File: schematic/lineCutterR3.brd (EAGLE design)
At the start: 55.9 x 30.5 mm, 53 parts, among them IC2 MC33269ST-3.3T3, J1 10118192-0001LF, Q1 AO4576, Q2 AO4576, Q3 DMG2305, Q4 AO4576, SW1 KMR2, U1 MS560702BA03-50, U2 MDBT50Q, U3 S25FL128SDPMFIG13S03016, U4 ESP32-S2-WROVER, U5 KXTJ3-1057, X1 2x5 0.05", X2 PIN-HEADER-MICRO-2-5-SMD

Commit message: Add Buck/Boost, RGB, Continuity, current sense
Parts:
- removed C20, C21, C5: .1u, rcl:C0805
- removed C3: 10u, rcl:C0805
- removed D1: MBR120, microbuilder:SOD-123
- removed IC2: MC33269ST-3.3T3, linear:SOT223
- removed JP1: JUMPER-SMT_2_NO_SILK, SparkFun-Jumpers:SMT-JUMPER_2_NO_SILK
- removed Q3: DMG2305, microbuilder:SOT23-R
- removed U5: KXTJ3-1057, Line Cutter COTS:KIONIX_KXTJ3-1057
- removed VCUT1, VCUT2: (no value), pinhead:1X02
- removed X2: PIN-HEADER-MICRO-2-5-SMD, freescale-uc:PIN-HEADER-NICRO-2-5-SMD
- added C10, C13, C14: 10u, rcl:C0805
- added C11, C15, C16: .1u, rcl:C0805
- added D2: XZM2CRKM2DGFBB45SCCB, SparkFun-LED:PLCC4SMDLED
- added D3: MBR120, microbuilder:SOD-123
- added H3, VCUT_1, VCUT_2: MOUNT-PAD-ROUND2.8, holes:2,8-PAD
- added L1: NR3015T1R5N, Line Cutter COTS:NR3015T1R5N
- added PS1: TPS63031DSKR, Line Cutter COTS:SON50P250X250X80-11N
- added Q5: DMG2305, microbuilder:SOT23-R
- added R18, R19, R20, R21: 10k, rcl:R0805
- added R22: 100k, rcl:R0805
- added R23, R24: 330, rcl:R0805
- added U6: ICM-20602, Line Cutter COTS:PQFN50P300X300X80-16N
- C9: value 4.7u -> .1u
- R17: value 100K -> 10k; device microbuilder:RESPACK_4X0603 -> rcl:R0805
- R7: value 10k -> 330
- U4: value ESP32-S2-WROVER -> ACS711KEXLT-31AB-T; device Line Cutter COTS:MODULE_ESP32-S2-WROVER -> Line Cutter COTS:SENSOR_ACS711KEXLT-31AB-T
- moved R7 204.8 mm to (-76.2, -177.2), flipped to the top
- moved C9 129.1 mm to (-52.7, -71.8), flipped to the top, turned to 0 degrees
- moved R16 107.3 mm to (78.7, -16.5), turned to 180 degrees
- moved R15 100.2 mm to (74.3, -16.5), turned to 180 degrees
- moved X1 87.6 mm to (7.62, 12.1), turned to 0 degrees
- moved SW1 84.6 mm to (14.0, 4.45), turned to 180 degrees
- moved R10 84.3 mm to (24.1, 22.2)
- moved R4 81.2 mm to (-32.4, 16.5), turned to 0 degrees
- moved CHG1 77.0 mm to (-32.4, 12.7), flipped to the bottom
- moved R9 76.9 mm to (19.1, 22.2)
- moved C12 74.9 mm to (-32.4, 8.89), turned to 180 degrees
- moved C1 74.7 mm to (74.3, 33.7), flipped to the top, turned to 180 degrees
- moved R3 73.4 mm to (-32.4, 3.81)
- moved CHG 69.9 mm to (-32.4, 6.35), turned to 90 degrees
- moved J1 67.6 mm to (22.4, 25.3), turned to 180 degrees
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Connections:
- removed net BL-RESET: R7.1, U4.41, X2.P$10
- removed net BOOT0: JP1.2, U4.3
- removed net IO38_DBLTAP: U4.32
- removed net TCK: U4.33, X2.P$4
- removed net TDI: U4.35, X2.P$8
- removed net TDO: U4.34, X2.P$6
- removed net TMS_D42: U4.36, X2.P$2
- removed net VHI: C20.2, C3.2, D1.C, IC2.3, Q3.2
- new net CUT_SENSE1: R18.1, R19.1, U2.9
- new net CUT_SENSE2: R20.1, R21.1, U2.20
- new net LED_B: R23.1, U2.44
- new net LED_G: R7.1, U2.42
- new net LED_R: R24.1, U2.41
- new net N$14: R17.1, U4.6
- new net N$15: D2.2, R7.2
- new net N$17: Q1.P$5, Q1.P$6, Q1.P$7, Q1.P$8, R18.2, VCUT_1.B2,8
- new net N$18: C11.2, PS1.6, PS1.7, PS1.8
- new net N$19: L1.2, PS1.4
- new net N$20: L1.1, PS1.2
- new net N$21: D2.1, R24.2
- new net N$22: C16.2, U6.14
- new net VBAT_IN_RAW: LIPO.1, Q4.P$4, U4.1
- new net VIN_REG1: C10.2, D3.C, PS1.5, Q5.2
- new net V_CURR_SENSE: U4.11
- net 3.3V: now also C13.2, C14.2, C15.2, PS1.1, PS1.10, R17.2, U4.12, U6.1, U6.16, U6.4, U6.5; no longer C21.2, C5.2, IC2.2, IC2.4, R7.2, U4.2, U5.10, U5.11, U5.3, U5.7, X2.P$1
- net CS0: no longer U4.20
- net CUT1: no longer U4.4
- net CUT2: no longer U4.5
- net GND: now also C10.1, C11.1, C13.1, C14.1, C15.1, C16.1, D2.4, PS1.11, PS1.3, PS1.9, R19.2, R21.2, R22.1, U4.10, U4.5, U4.7, U4.8, U4.9, U6.10, U6.11, U6.12, U6.13, U6.15, U6.8, U6.9; no longer C20.1, C21.1, C3.1, C5.1, IC2.1, JP1.1, R17.8, U4.1, U4.26, U4.42, U4.43_1, U4.43_10, U4.43_11, U4.43_12, U4.43_13, U4.43_14, U4.43_15, U4.43_16, U4.43_17, U4.43_18, U4.43_19, U4.43_2, U4.43_20, U4.43_21, U4.43_3, U4.43_4, U4.43_5, U4.43_6, U4.43_7, U4.43_8, U4.43_9, U5.1, U5.4, U5.6, U5.8, U5.9, X2.P$3, X2.P$5, X2.P$7, X2.P$9
- net MISO: no longer U4.31
- net MOSI: no longer U4.29
- net N$16: now also D2.3, R23.2; no longer Q1.P$5, Q1.P$6, Q1.P$7, Q1.P$8, VCUT1.1
- net N$6: now also R20.2, VCUT_2.B2,8; no longer VCUT2.1
- net SCK: no longer U4.30
- net SCL: now also U6.2; no longer U4.28, U5.12
- net SDA: now also U6.3; no longer U4.27, U5.2
- net USB_D+: no longer U4.23
- net USB_D-: no longer U4.22
- net VBAT: now also H3.B2,8, Q5.3, U4.3; no longer LIPO.1, Q3.3, Q4.P$4, VCUT1.2, VCUT2.2
- net VUSB: now also D3.A, Q5.1, R22.2; no longer D1.A, Q3.1, R17.1
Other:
- board size 55.9 x 30.5 mm -> 50.8 x 29.2 mm

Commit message: final code for cert rocket tests
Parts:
- moved C12 67.3 mm to (34.9, 8.89)
- moved CHG 67.3 mm to (34.9, 6.35)
- moved CHG1 67.3 mm to (34.9, 12.7)
- moved R3 67.3 mm to (34.9, 3.81)
- moved R4 67.3 mm to (34.9, 16.5)
- moved D3 45.3 mm to (43.2, 10.5)
- moved PS1 45.2 mm to (43.8, 13.3)
- moved Q5 44.5 mm to (43.8, 8.00)
- moved L1 44.3 mm to (39.4, 14.0)
- moved C1 43.2 mm to (39.4, 8.26)
- moved Q2 19.7 mm to (18.4, 3.81)
- moved D2 3.59 mm to (34.9, 20.3)
- moved U1 3.59 mm to (30.5, 14.6), turned to 180 degrees
- moved Q1 3.24 mm to (10.8, 3.81)
- moved SW1 3.24 mm to (10.8, 3.81)
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
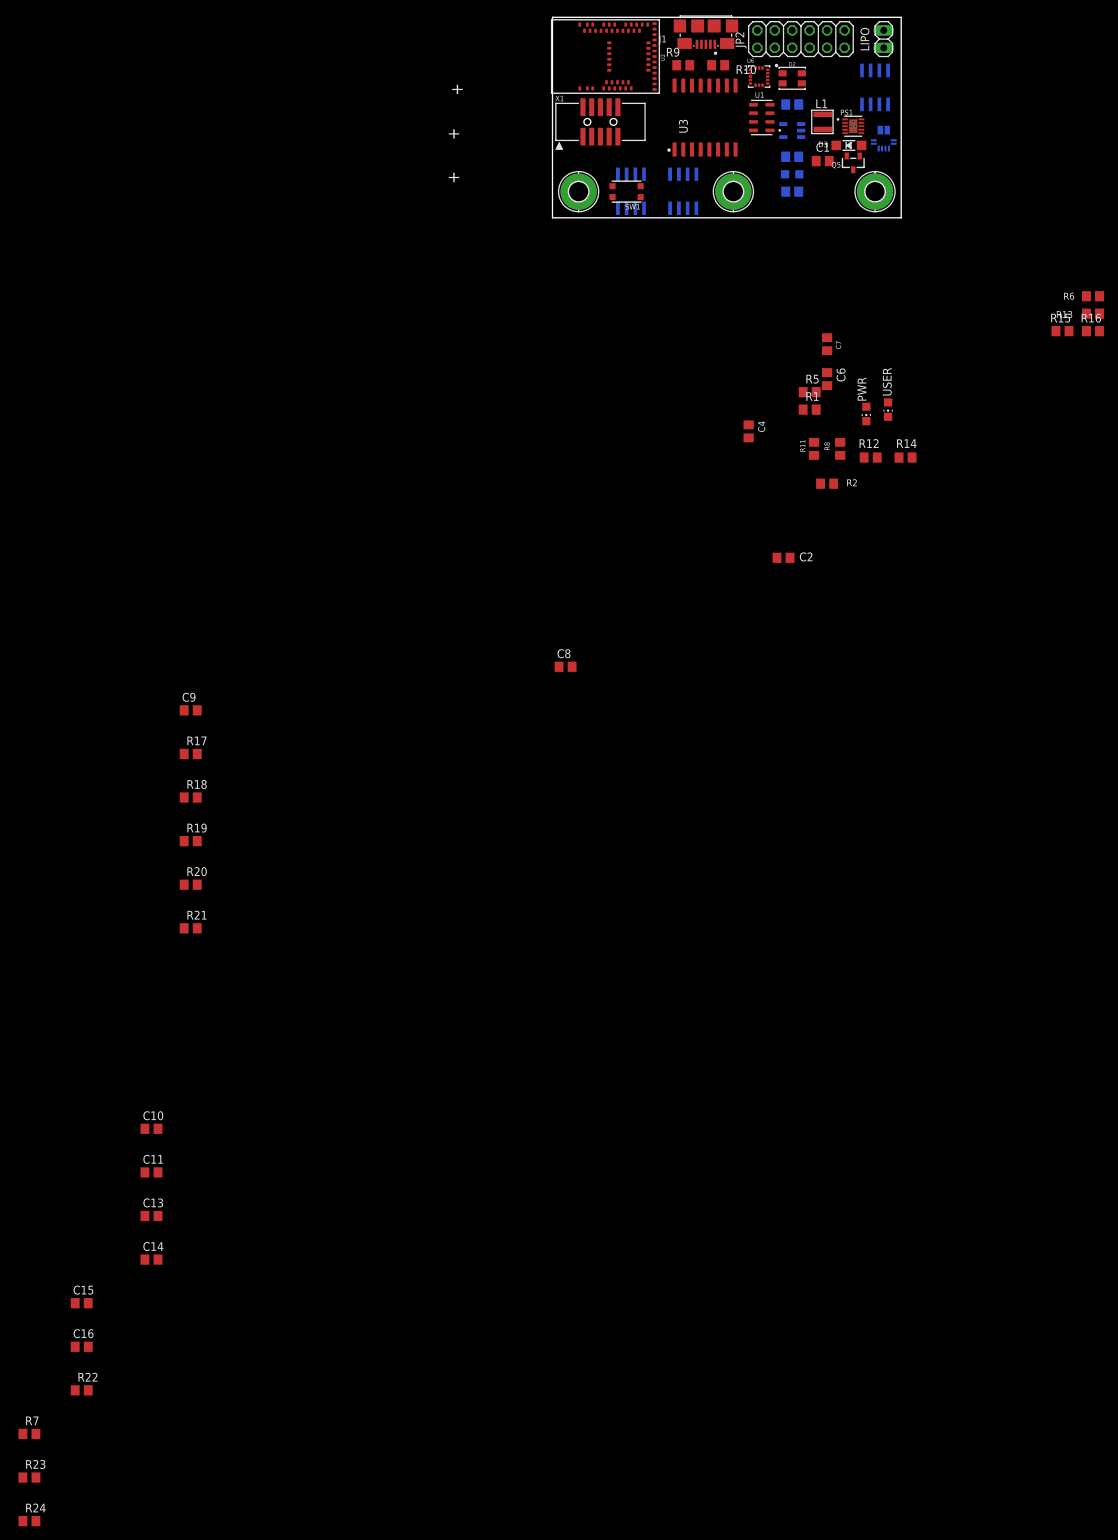
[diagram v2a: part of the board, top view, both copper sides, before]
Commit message: R3 PCB: Place most of the components
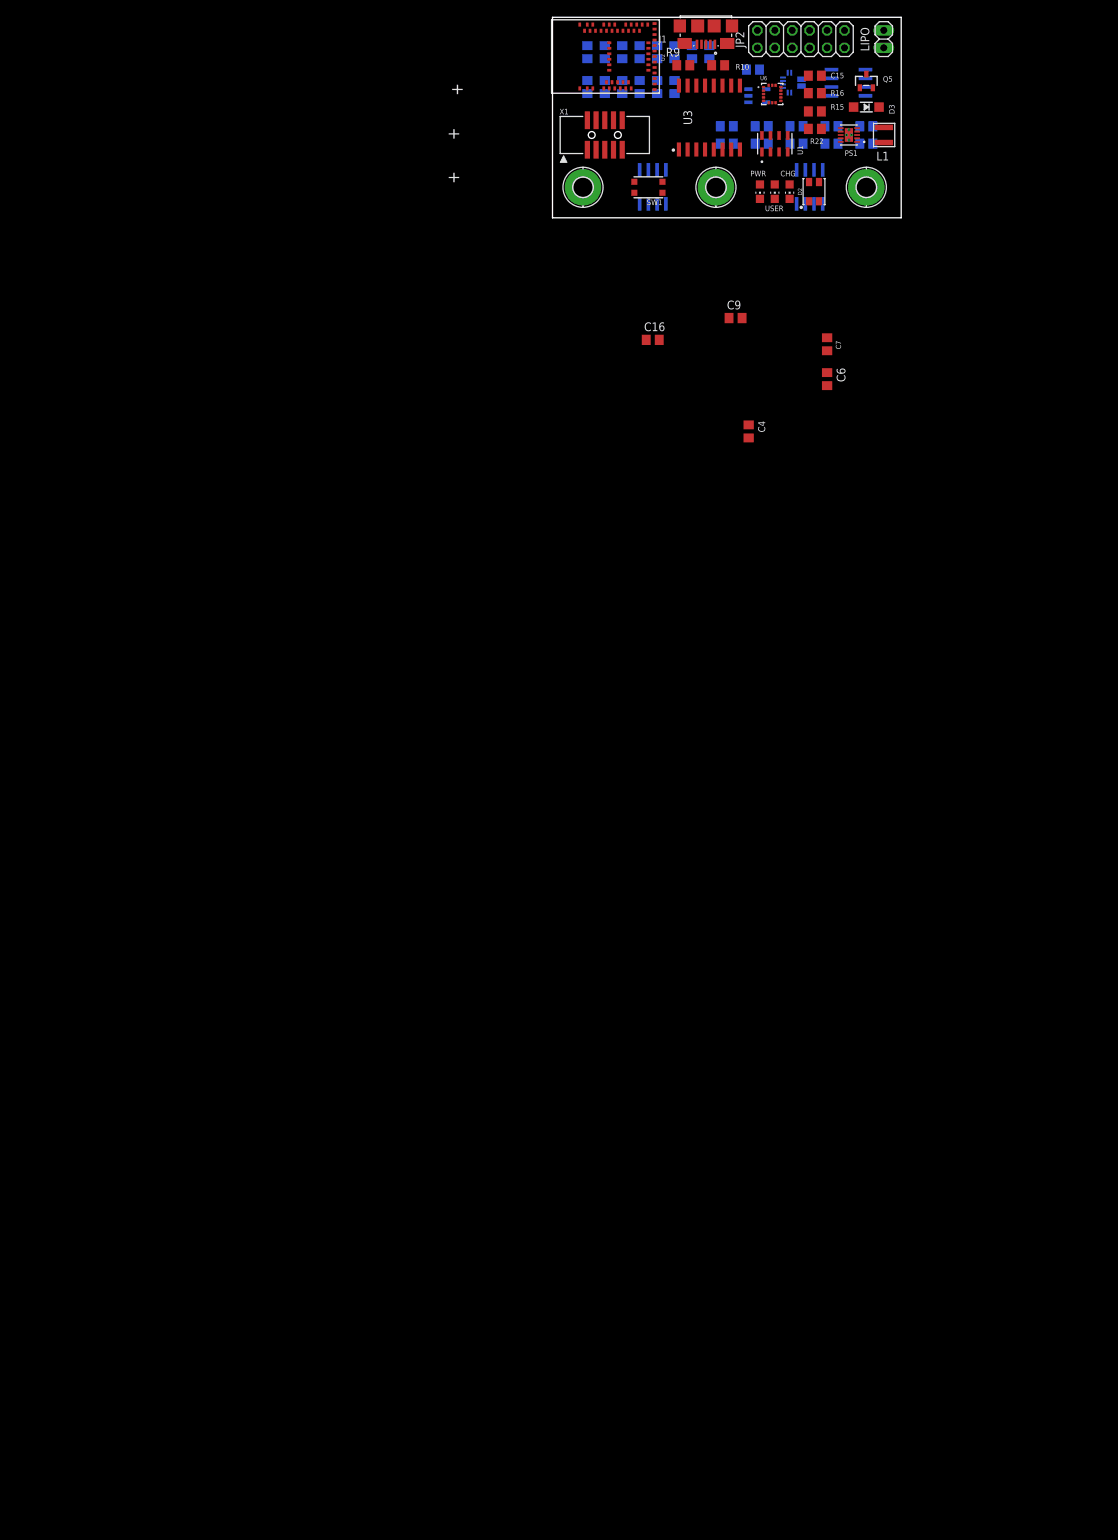
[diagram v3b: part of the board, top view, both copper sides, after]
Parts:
- removed C2: NF, rcl:C0805
- removed R2: NF, rcl:R0805
- moved R24 229.8 mm to (7.62, 24.1), flipped to the bottom, turned to 270 degrees
- moved R23 224.9 mm to (10.2, 24.1), flipped to the bottom, turned to 270 degrees
- moved R7 217.1 mm to (5.08, 24.1), flipped to the bottom, turned to 270 degrees
- moved R22 212.6 mm to (38.2, 13.0)
- moved C15 206.1 mm to (38.2, 18.2)
- moved C14 195.2 mm to (45.7, 13.3), flipped to the bottom
- moved C13 187.7 mm to (45.7, 10.8), flipped to the bottom
- moved C11 179.6 mm to (40.6, 10.8), flipped to the bottom
- moved C10 176.5 mm to (40.6, 13.3), flipped to the bottom
- moved C16 168.6 mm to (14.6, -17.8)
- moved R21 141.4 mm to (17.8, 19.1), flipped to the bottom, turned to 270 degrees
- moved R20 134.6 mm to (15.2, 19.1), flipped to the bottom, turned to 270 degrees
- moved R17 129.0 mm to (29.2, 21.6), flipped to the bottom
- moved R19 127.9 mm to (12.7, 19.1), flipped to the bottom, turned to 270 degrees
- moved R18 121.1 mm to (10.2, 19.1), flipped to the bottom, turned to 270 degrees
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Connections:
- removed net N$2: C2.2, J1.SH1, J1.SH2, J1.SH3, J1.SH4, J1.SH5, J1.SH6, R2.1
- net GND: now also J1.SH1, J1.SH2, J1.SH3, J1.SH4, J1.SH5, J1.SH6; no longer C2.1, R2.2
- net V_CURR_SENSE: now also U2.21

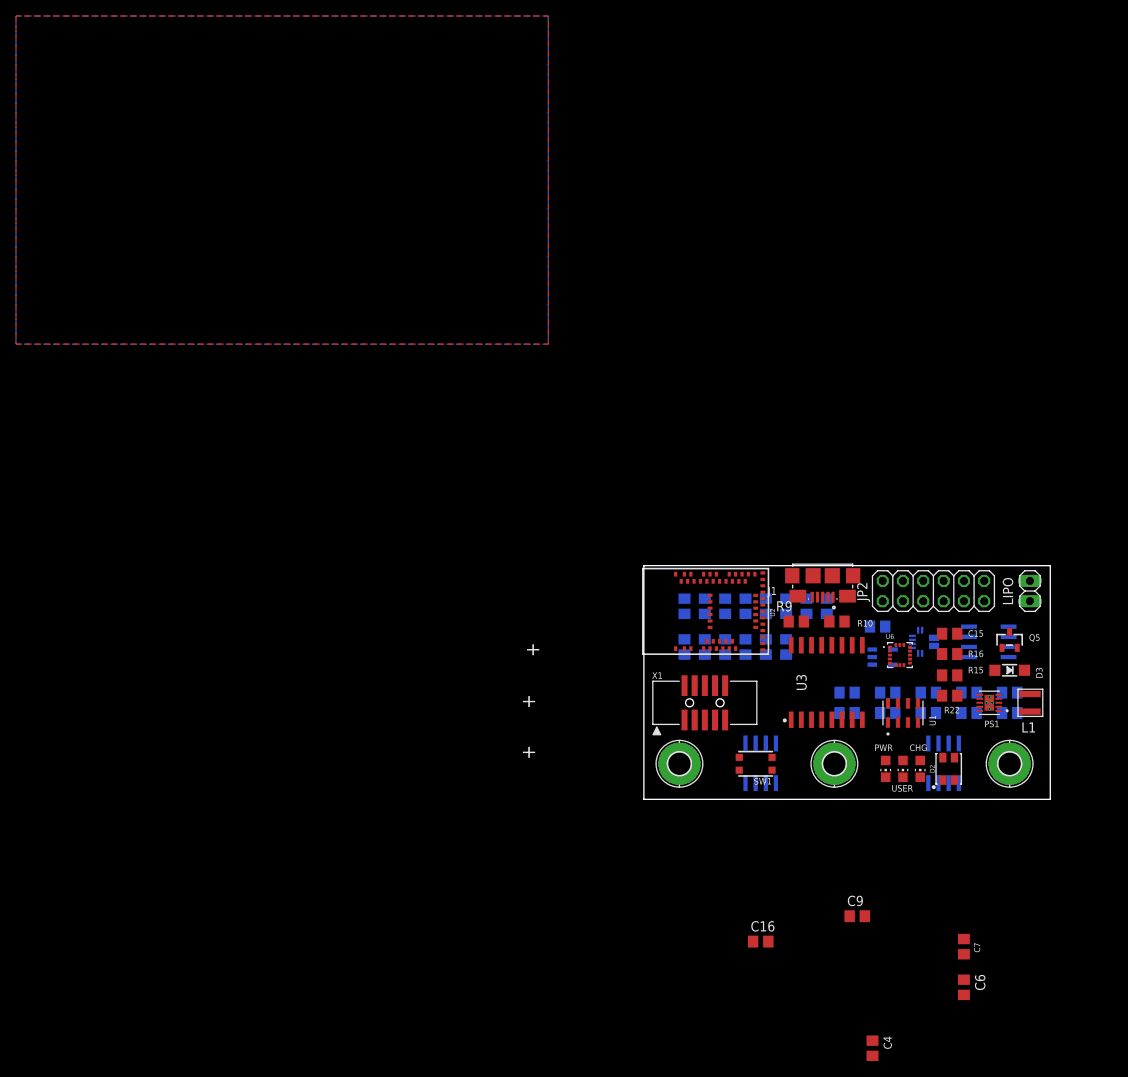
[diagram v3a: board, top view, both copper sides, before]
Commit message: Pass 1 at routing line cutter R3
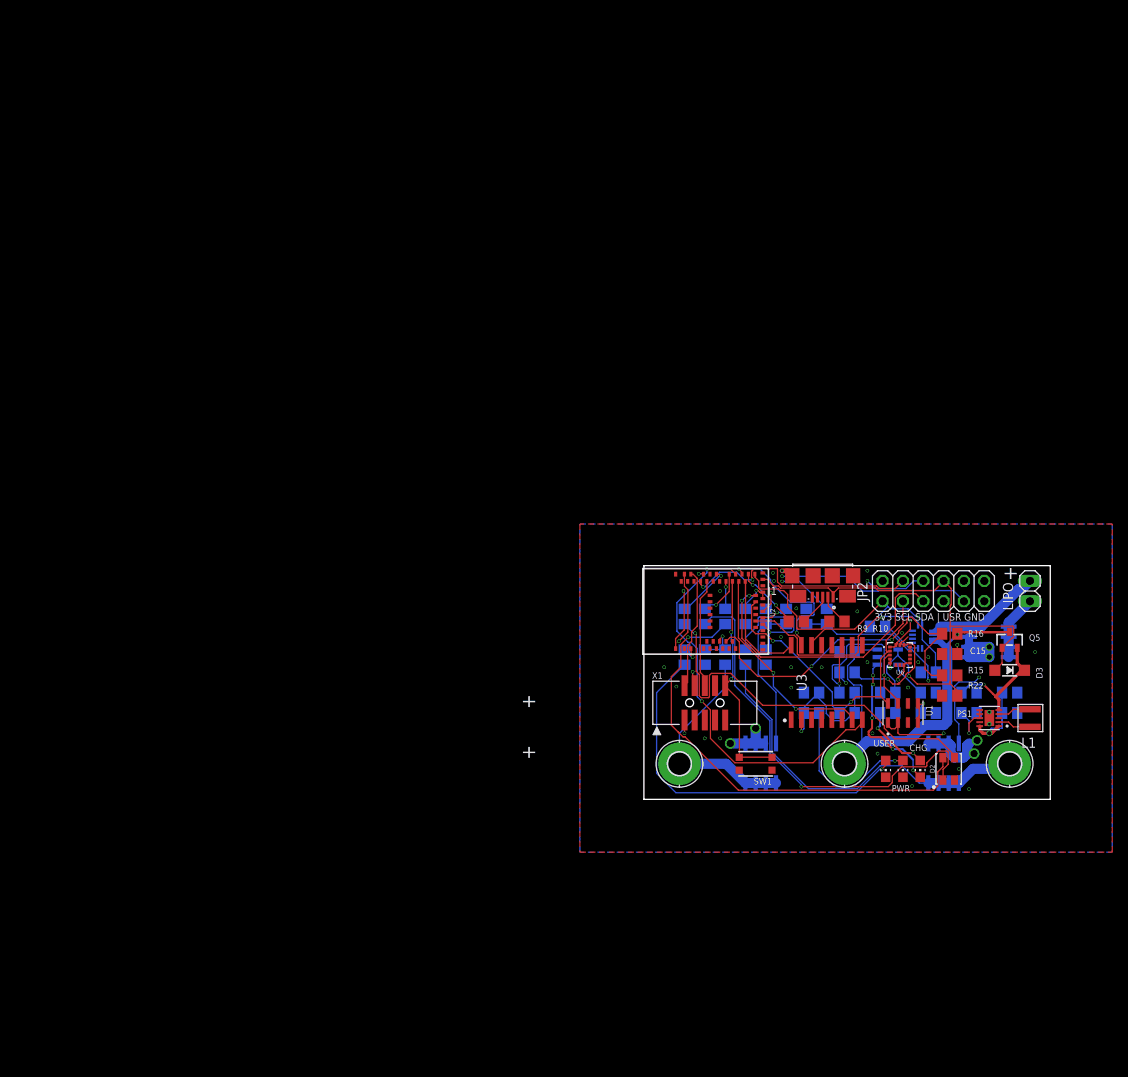
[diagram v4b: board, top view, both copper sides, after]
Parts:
- removed C6: .1u, rcl:C0805
- moved C4 49.6 mm to (25.4, 18.4), flipped to the bottom, turned to 0 degrees
- moved C7 37.0 mm to (21.0, 13.3), flipped to the bottom, turned to 180 degrees
- moved C16 35.3 mm to (25.4, 15.9), flipped to the bottom, turned to 180 degrees
- moved C9 31.8 mm to (35.6, 15.9), flipped to the bottom
- moved R11 17.9 mm to (21.0, 10.8), turned to 180 degrees
- moved R23 5.24 mm to (5.08, 22.9)
- moved R7 5.24 mm to (10.2, 22.9)
- moved R19 5.24 mm to (7.62, 17.8)
- moved R20 2.84 mm to (12.7, 17.8)
- moved R21 2.84 mm to (15.2, 17.8)
- moved R8 2.84 mm to (5.08, 17.8)
- moved PWR 2.16 mm to (32.4, 3.81)
- moved USER 2.16 mm to (30.2, 3.81)
- moved L1 1.90 mm to (48.3, 10.2)
- moved PS1 1.90 mm to (43.2, 10.2)
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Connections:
- removed net N$13: JP2.7
- net 3.3V: no longer C6.2
- net CUT1: no longer R1.1
- net CUT2: no longer R5.1
- net GND: no longer C6.1
- net N$10: now also R1.1
- net N$3: now also R5.1
- net N$7: now also USER.A; no longer PWR.A
- net N$9: now also PWR.A; no longer USER.A
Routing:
- net 3.3V: track 0.00 -> 86.6 mm, vias 0 -> 10
- net VUSB: track 0.00 -> 73.1 mm, vias 0 -> 1
- net SDA: track 0.00 -> 62.6 mm, vias 0 -> 4
- net N$15: track 0.00 -> 58.2 mm, vias 0 -> 1
- net VBAT: track 0.00 -> 54.9 mm, vias 0 -> 1
- net N$21: track 0.00 -> 53.3 mm, vias 0 -> 1
- net MISO: track 0.00 -> 51.2 mm, vias 0 -> 2
- net N$16: track 0.00 -> 49.4 mm, vias 0 -> 1
- net N$6: track 0.00 -> 47.0 mm
- net N$7: track 0.00 -> 46.7 mm, vias 0 -> 1
- net BATT_SENSE: track 0.00 -> 42.5 mm, vias 0 -> 2
- net USER: track 0.00 -> 42.4 mm, vias 0 -> 2
- net SCL: track 0.00 -> 40.9 mm, vias 0 -> 2
- net GND: track 0.00 -> 38.1 mm, vias 0 -> 34
- net N$3: track 0.00 -> 36.7 mm, vias 0 -> 2
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- added copper zone on layer 2, net A
- added copper zone on layer 15, net A1
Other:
- board text added: "3V3 SCL SDA | USR GND"
- board text added: "Matt Morley | AeroNU"
- board text removed: "Designed by Matthew Morley"

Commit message: Update lineCutterR3.brd
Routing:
- net GND: track 38.1 -> 31.9 mm, vias 34 -> 48
- net N$11: track 8.23 -> 9.16 mm, vias 2 -> 0
- net N$12: track 15.1 -> 14.2 mm
- net BATT_SENSE: track 42.5 -> 41.7 mm
- net N$7: track 46.7 -> 47.4 mm
- net N$3: track 36.7 -> 37.3 mm
- net MISO: track 51.2 -> 51.8 mm
- net 3.3V: track 86.6 -> 87.1 mm
